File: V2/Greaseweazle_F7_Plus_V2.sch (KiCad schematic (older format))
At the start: 62 parts, among them J1 Wurth 694106301002, J10 PIN1X2, J11 PIN1X2, J12 IDC Box Header, J2 USB_B, J3 Molex 105017-1001, J4 TE EI 171826-4, J5 PIN1X3, J6 PIN1X2, J7 PIN1X5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

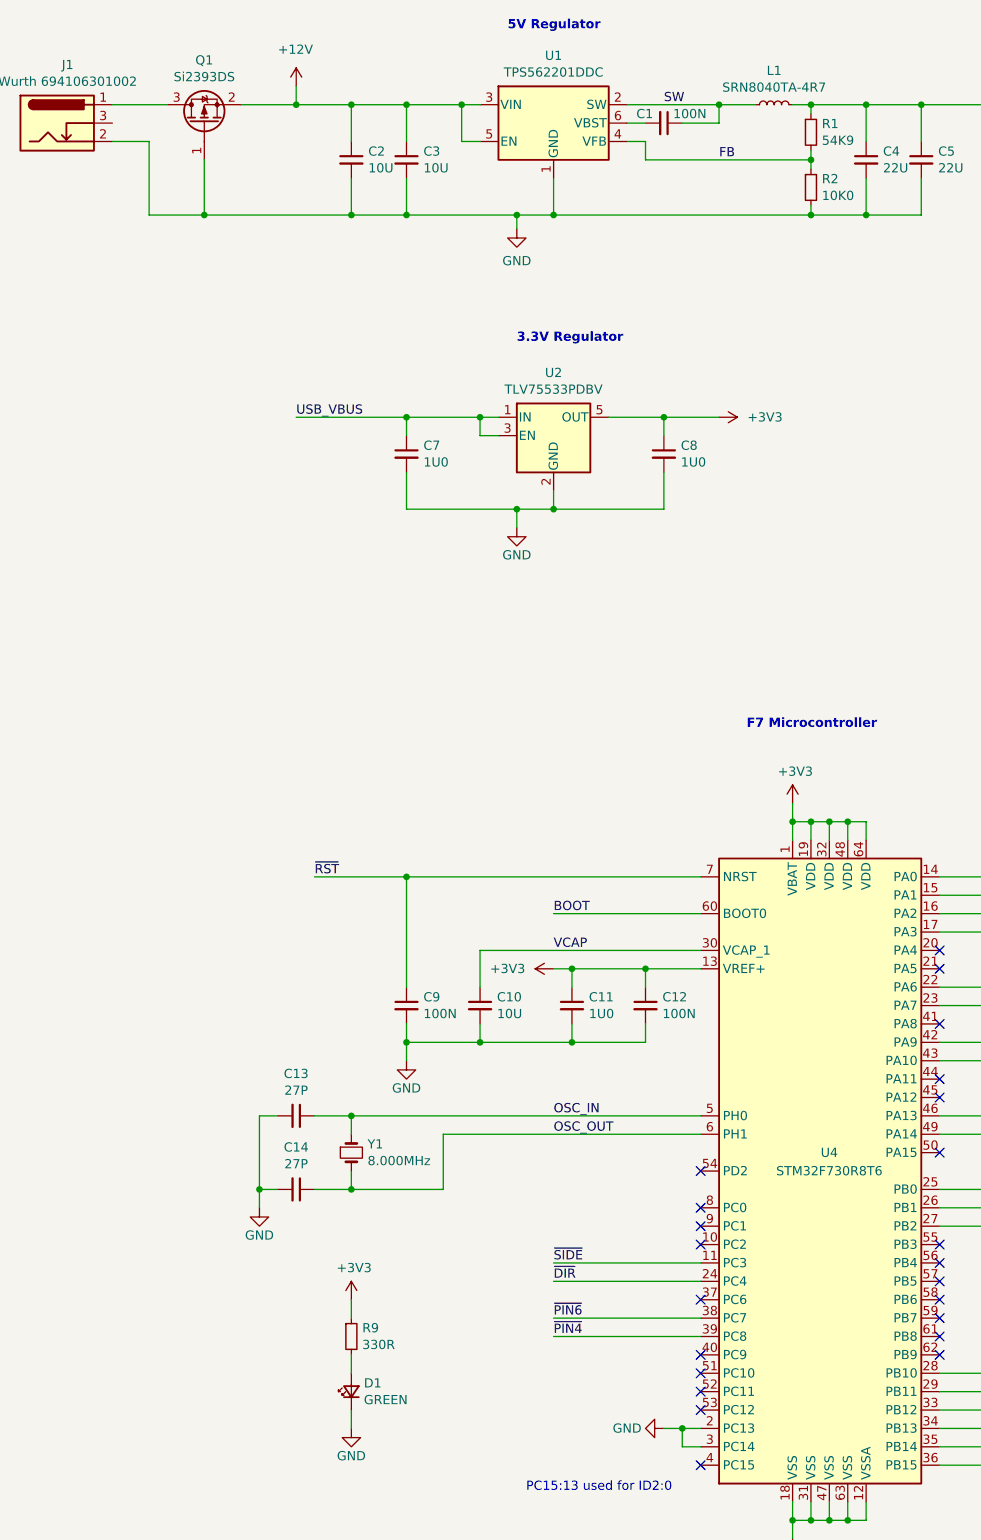
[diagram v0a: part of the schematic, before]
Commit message: added JLCPBC component ids, adapted footprints changed components which are no available in JLCPCB catalog
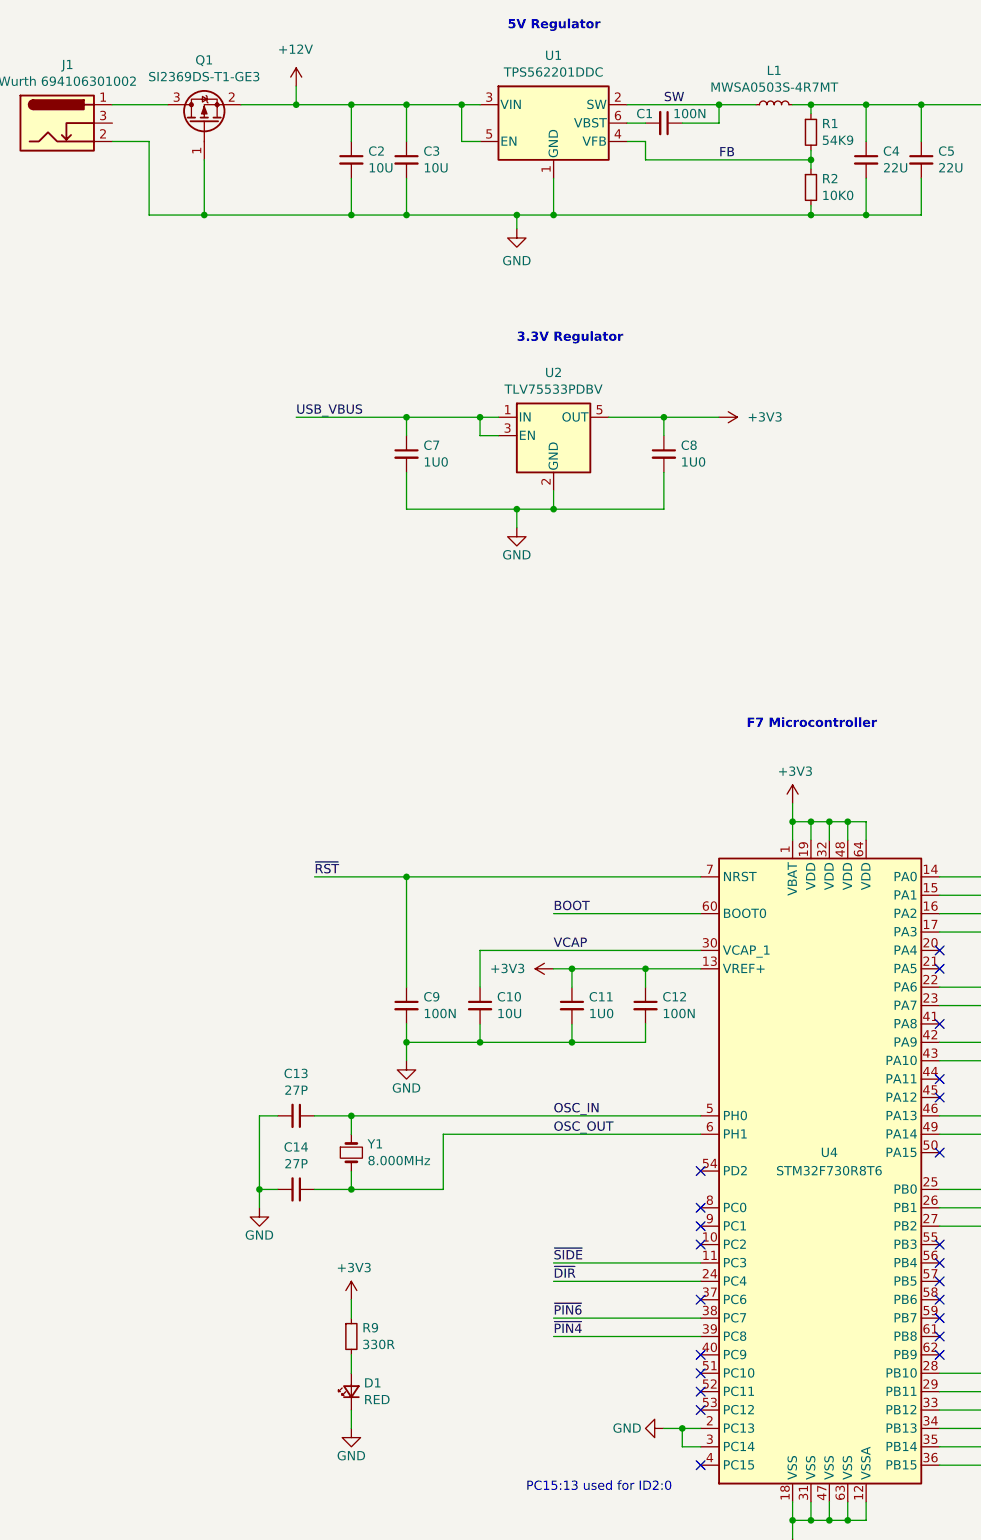
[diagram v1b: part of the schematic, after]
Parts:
- C1, C12, C15, C16, C17, C18, C19, C20, C6, C9: footprint Capacitor_SMD:C_0805_2012Metric_Pad1.15x1.40mm_HandSolder -> Capacitor_SMD:C_0402_1005Metric; LCSC (none) -> C1525; MFR.Part (none) -> CL05B104KO5NNNC
- C10, C2, C3: footprint Capacitor_SMD:C_0805_2012Metric_Pad1.15x1.40mm_HandSolder -> Capacitor_SMD:C_0805_2012Metric; LCSC (none) -> C15850; MFR.Part (none) -> CL21A106KAYNNNE
- C11, C7, C8: footprint Capacitor_SMD:C_0805_2012Metric_Pad1.15x1.40mm_HandSolder -> Capacitor_SMD:C_0402_1005Metric; LCSC (none) -> C52923; MFR.Part (none) -> CL05A105KA5NQNC
- C13, C14: footprint Capacitor_SMD:C_0805_2012Metric_Pad1.15x1.40mm_HandSolder -> Capacitor_SMD:C_0402_1005Metric; LCSC (none) -> C1557; MFR.Part (none) -> 0402CG270J500NTN
- C4, C5: footprint Capacitor_SMD:C_0805_2012Metric_Pad1.15x1.40mm_HandSolder -> Capacitor_SMD:C_0805_2012Metric; LCSC (none) -> C45783; MFR.Part (none) -> CL21A226MAQNNNE
- D1: value GREEN -> RED; footprint LED_SMD:LED_0805_2012Metric_Pad1.15x1.40mm_HandSolder -> LED_SMD:LED_0603_1608Metric; LCSC (none) -> C2286; MFR.Part (none) -> KT-0603R
- D2: footprint LED_SMD:LED_0805_2012Metric_Pad1.15x1.40mm_HandSolder -> LED_SMD:LED_0603_1608Metric; LCSC (none) -> C72043; MFR.Part (none) -> 19-217/GHC-YR1S2/3T
- L1: value SRN8040TA-4R7 -> MWSA0503S-4R7MT; footprint Inductor_SMD:L_Bourns_SRN8040TA -> greaseweazle:L_5.4x5.2_H2.8; LCSC (none) -> C408410; MFR.Part (none) -> MWSA0503S-4R7MT
- Q1: value Si2393DS -> SI2369DS-T1-GE3; LCSC (none) -> C141546; MFR.Part (none) -> SI2369DS-T1-GE3
- R1: footprint Resistor_SMD:R_0805_2012Metric_Pad1.15x1.40mm_HandSolder -> Resistor_SMD:R_0603_1608Metric; LCSC (none) -> C23077; MFR.Part (none) -> 0603WAF5492T5E
- R10, R9: footprint Resistor_SMD:R_0805_2012Metric_Pad1.15x1.40mm_HandSolder -> Resistor_SMD:R_0805_2012Metric; LCSC (none) -> C17630; MFR.Part (none) -> 0805W8F3300T5E
- R11, R12: footprint Resistor_SMD:R_0805_2012Metric_Pad1.15x1.40mm_HandSolder -> Resistor_SMD:R_0805_2012Metric; LCSC (none) -> C28636; MFR.Part (none) -> 0805W8F5600T5E
- R2, R4: footprint Resistor_SMD:R_0805_2012Metric_Pad1.15x1.40mm_HandSolder -> Resistor_SMD:R_0603_1608Metric; LCSC (none) -> C25804; MFR.Part (none) -> 0603WAF1002T5E
- R3, R5, R6, R7, R8: footprint Resistor_SMD:R_0805_2012Metric_Pad1.15x1.40mm_HandSolder -> Resistor_SMD:R_0805_2012Metric; LCSC (none) -> C17513; MFR.Part (none) -> 0805W8F1001T5E
- U1: LCSC (none) -> C90061; MFR.Part (none) -> TPS562201DDCR
- U2: LCSC (none) -> C404027; MFR.Part (none) -> TLV75533PDBVR
- U3: LCSC (none) -> C7519; MFR.Part (none) -> USBLC6-2SC6
- U4: LCSC (none) -> C478453; MFR.Part (none) -> STM32F730R8T6
- U5, U6: LCSC (none) -> C6801; MFR.Part (none) -> SN74LS07DRG4
- Y1: LCSC (none) -> C115962; MFR.Part (none) -> X50328MSB2GI

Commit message: made autorouting possible use components which are in stock on JLCPCB
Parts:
- added H5, H6: ToolHole, greaseweazle:ToolingHole_1.152mm, symbol Mechanical:MountingHole
- added U10, U7, U8, U9: NarrowPowerAdapter, greaseweazle:NarrowPowerAdapter_0.60_to_0.25, symbol greaseweazle:NarrowPowerAdapter
- U3: value USBLC6-2SC6 -> TPUSBLC6-2SC6; LCSC C7519 -> C558442; MFR.Part USBLC6-2SC6 -> TPUSBLC6-2SC6
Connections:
- net +12V: now also U9.1 (Normal); no longer U1.5 (EN)
- net +3V3: now also U10.1 (Normal), U8.1 (Normal); no longer U4.1 (VBAT), U4.13 (VREF+), U4.19 (VDD), U4.32 (VDD), U4.48 (VDD), U4.64 (VDD)
- net GND: now also U3.2 (GND), U7.1 (Normal); no longer U4.12 (VSSA), U4.18 (VSS), U4.2 (PC13), U4.3 (PC14), U4.31 (VSS), U4.47 (VSS), U4.63 (VSS)
- net USB_D+: now also U3.4 (I/O2)
- net USB_D-: now also U3.6 (I/O1)
- net USB_DIN+: now also U3.3 (I/O2)
- net USB_DIN-: now also U3.1 (I/O1)
- net USB_VBUS: now also U3.5 (VBUS)
- net 12V_conn: now reaches J1.1, Q1.3 (D)
- new net: U4.1 (VBAT), U4.19 (VDD), U4.32 (VDD), U4.48 (VDD), U4.64 (VDD), U8.2 (Narrow)
- new net: U4.12 (VSSA), U4.18 (VSS), U4.2 (PC13), U4.3 (PC14), U4.31 (VSS), U4.47 (VSS), U4.63 (VSS), U7.2 (Narrow)
- new net: U10.2 (Narrow), U4.13 (VREF+)
- new net: U1.5 (EN), U9.2 (Narrow)
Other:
- moved on the sheet: C10, C11, C12, C9

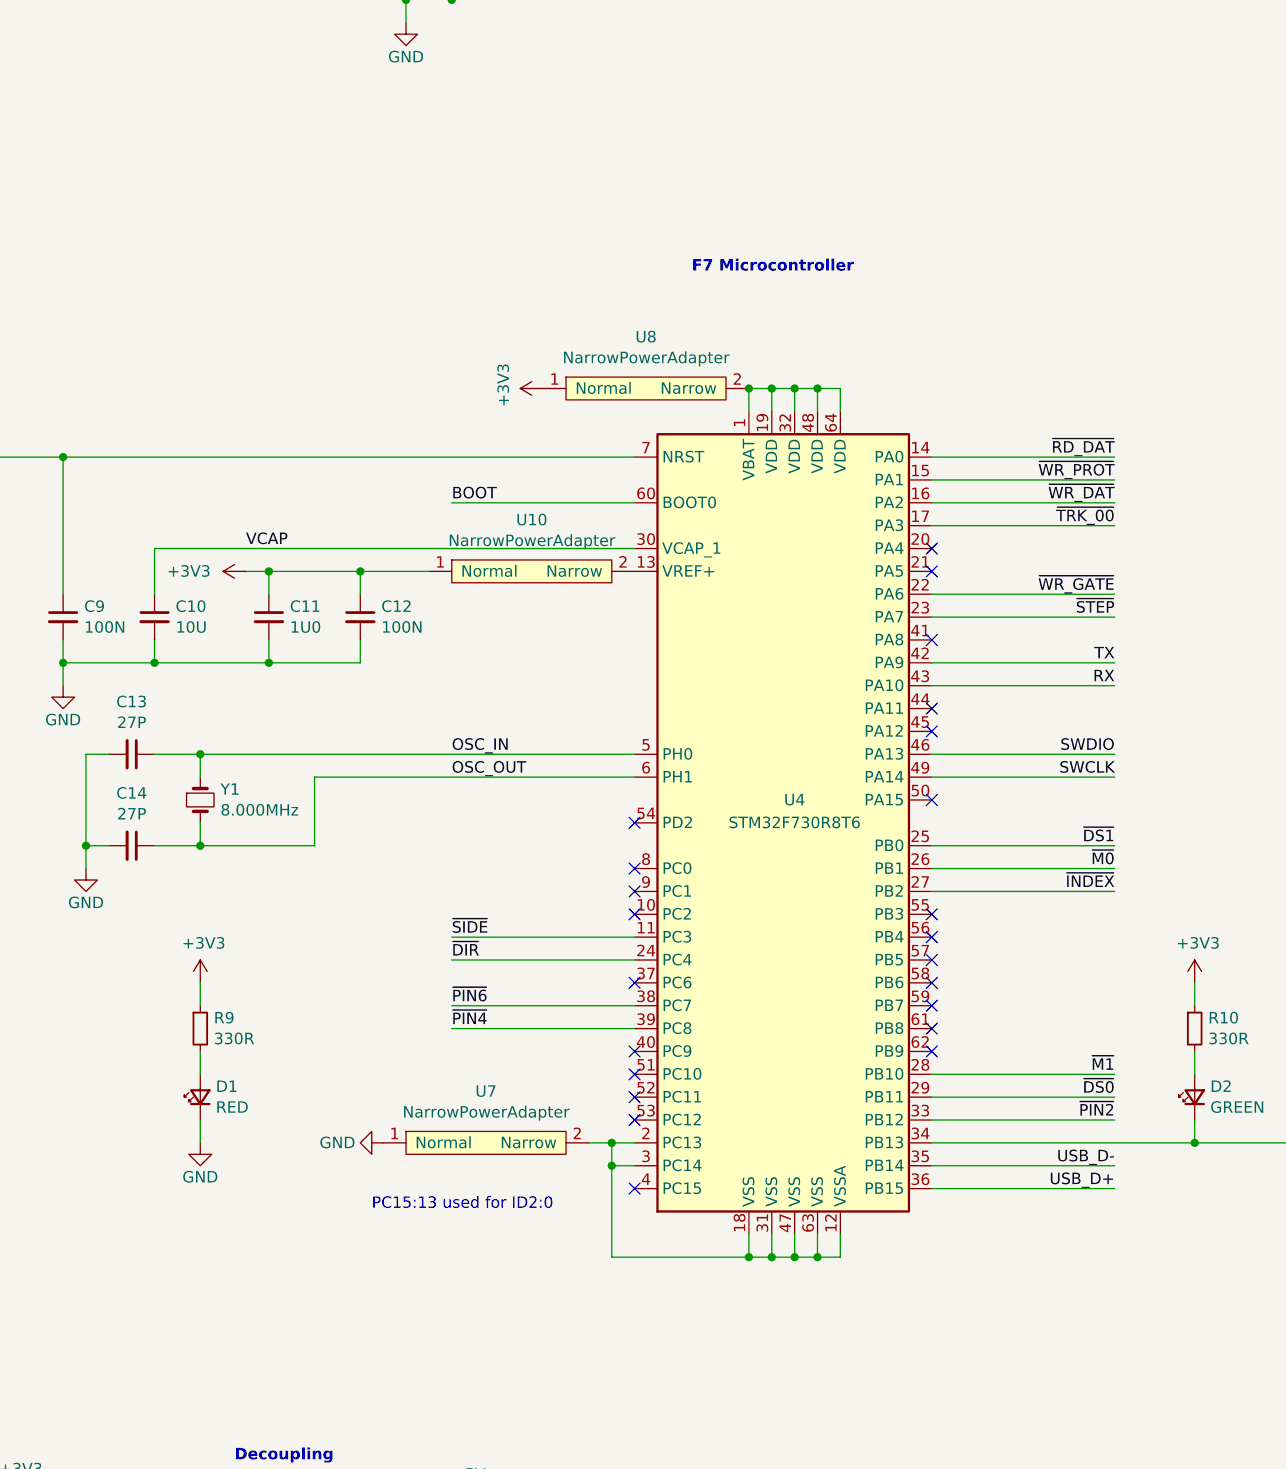
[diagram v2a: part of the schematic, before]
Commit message: added copper fill below mcu and L1 improved power connections of mcu
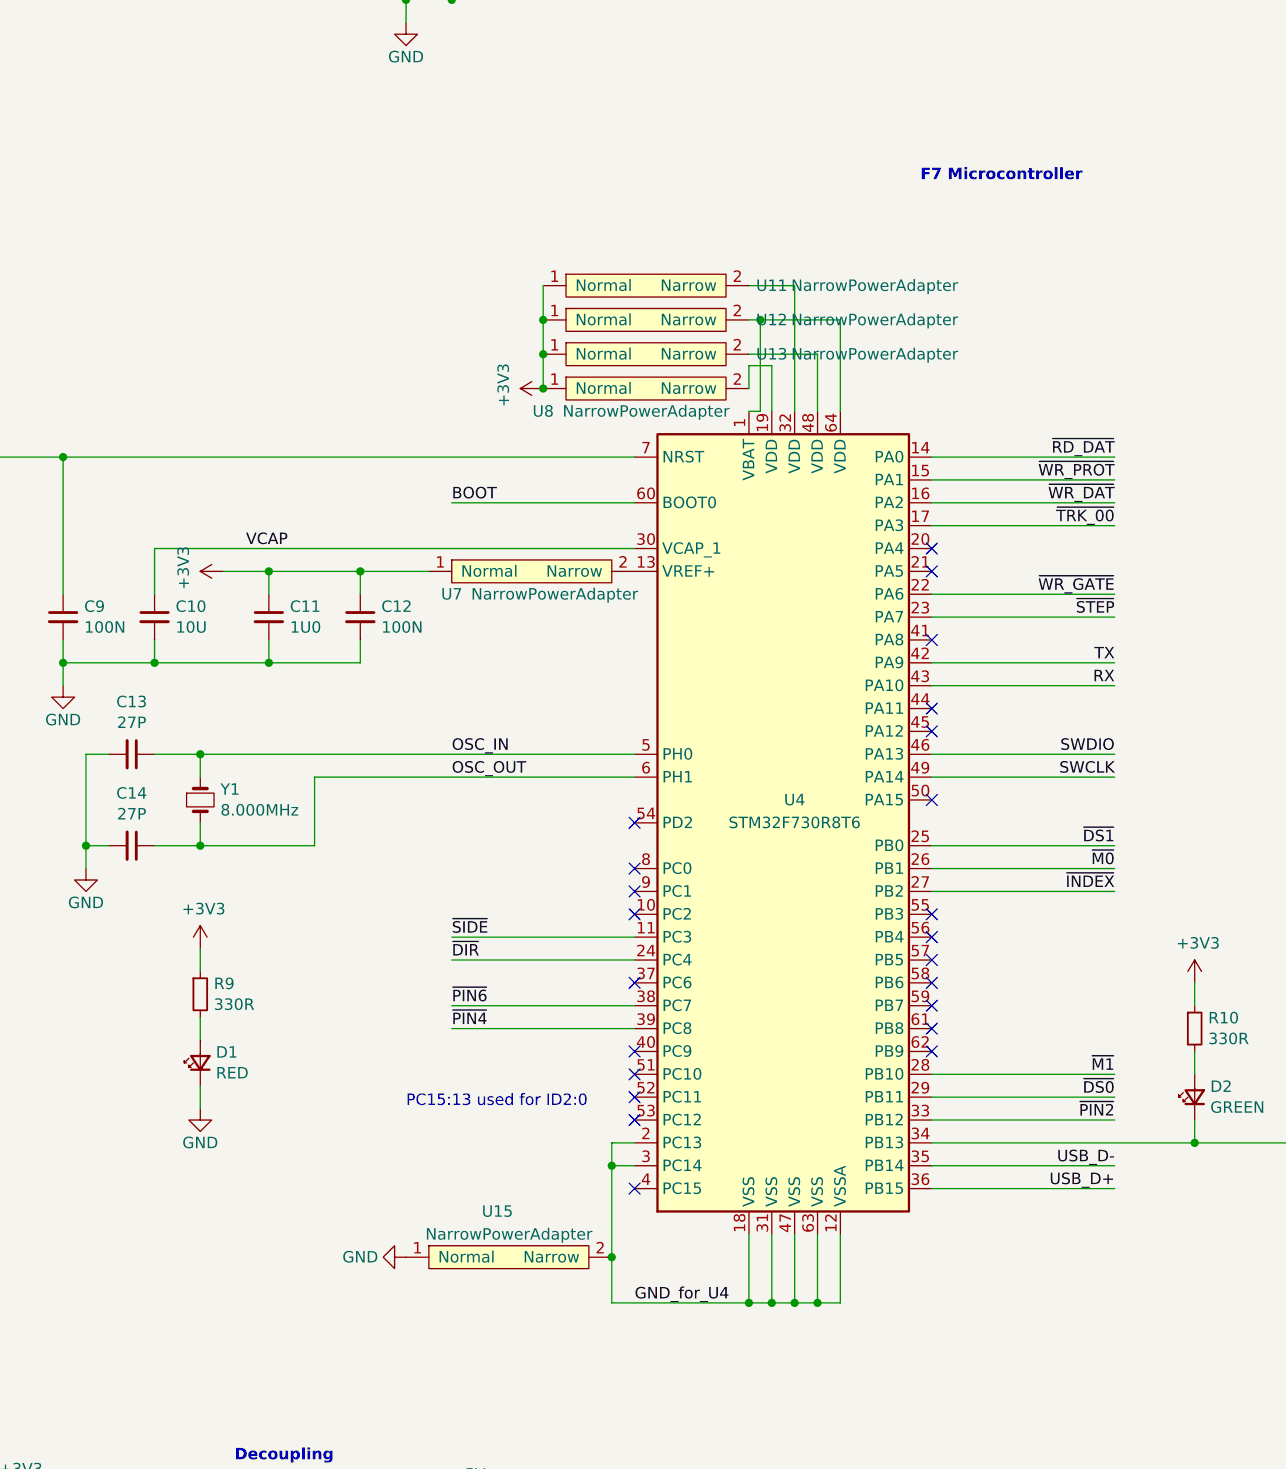
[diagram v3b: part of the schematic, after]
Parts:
- removed U10: NarrowPowerAdapter, greaseweazle:NarrowPowerAdapter_0.60_to_0.25, symbol greaseweazle:NarrowPowerAdapter
- added U11, U12, U13: NarrowPowerAdapter, greaseweazle:NarrowPowerAdapter_0.60_to_0.25, symbol greaseweazle:NarrowPowerAdapter
- added U15: NarrowPowerAdapter, greaseweazle:NarrowPowerAdapter_0.60_to_0.25_thick, symbol greaseweazle:NarrowPowerAdapter
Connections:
- net +3V3: now also U7.1 (Normal), U11.1 (Normal), U12.1 (Normal), U13.1 (Normal)
- net GND: now also U15.1 (Normal); no longer U7.1 (Normal)
- net GND_for_U4: now reaches U4.12 (VSSA), U4.18 (VSS), U4.2 (PC13), U4.3 (PC14), U4.31 (VSS), U4.47 (VSS), U4.63 (VSS)
- net GND_for_U4: now also U15.2 (Narrow); no longer U7.2 (Narrow)
- net at U4.13 (VREF+): now also U7.2 (Narrow)
- new net: U12.2 (Narrow), U4.1 (VBAT), U4.64 (VDD)
- new net: U4.19 (VDD), U8.2 (Narrow)
- new net: U11.2 (Narrow), U4.32 (VDD)
- new net: U13.2 (Narrow), U4.48 (VDD)
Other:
- moved on the sheet: D1, R9
